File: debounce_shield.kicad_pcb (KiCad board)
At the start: 2 copper layers, 65 x 56 mm, 39 parts, among them J2 RPi_GPIO, P1 CONN_12, P2 CONN_2, U1 40106

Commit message: Add HAT EEPROM & 5V feed diode.
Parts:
- added D7: DIODE, Diodes_SMD:D_0805, F.Cu at (153.0, 81.0)
- added K1: CONN_3, Pin_Headers:Pin_Header_Straight_1x03_Pitch2.54mm, F.Cu at (106.3, 94.5)
- added R19: 1k, Resistors_SMD:R_0805_HandSoldering, F.Cu at (107.8, 82.9)
- added U2: CAT24C32, SMD_Packages:SOIC-8-N, F.Cu at (112.8, 91.6)
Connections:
- J2 pad 2: Net-(J2-Pad2) -> Net-(D7-Pad2)
- J2 pad 27: (no net) -> IDSDA
- J2 pad 28: (no net) -> IDSCL
- J2 pad 4: Net-(J2-Pad2) -> Net-(D7-Pad2)
- P2 pad 2: Net-(J2-Pad2) -> Net-(D7-Pad1)
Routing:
- net Net-(D7-Pad2): track 0.00 -> 62.6 mm
- net Net-(J2-Pad2): track 60.2 -> 0.00 mm
- net IDSCL: track 0.00 -> 40.2 mm, vias 0 -> 1
- net IDSDA: track 0.00 -> 29.1 mm, vias 0 -> 3
- net GND: track 12.5 -> 38.8 mm, vias 7 -> 8
- net +3.3V: track 119.9 -> 105.1 mm
- net Net-(K1-Pad2): track 0.00 -> 8.88 mm
- net Net-(K1-Pad3): track 0.00 -> 6.59 mm
- net Net-(D7-Pad1): track 0.00 -> 4.68 mm
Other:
- net class Power5V added: clearance 0.2, trace_width 0.6, via_dia 0.6, via_drill 0.4

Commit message: Update documentation.
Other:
- board text added: "Wr - WP"
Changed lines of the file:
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@@
     (links 89)
     (no_connects 0)
-    (area 87.089172 61.3852 190.182029 141.5602)
+    (area 97.460599 72.493818 162.560601 128.635201)
     (thickness 1.6)
-    (drawings 28)
+    (drawings 29)
     (tracks 303)
     (zones 0)
@@
   )
   (setup
-    (last_trace_width 0.6)
+    (last_trace_width 0.25)
     (user_trace_width 0.01)
     (user_trace_width 0.02)
@@
       (rotate (xyz 0 0 0))
     )
+  )
+  (gr_text "Wr - WP" (at 108.8898 92.0877 90) (layer F.SilkS)
+    (effects (font (size 1 1) (thickness 0.2)))
   )
   (gr_text "GND +5V" (at 161.798 83.6549 90) (layer F.SilkS)
@@
   (segment (start 153.1788 82.1817) (end 153.0096 82.0125) (width 0.6) (layer F.Cu) (net 31))
   (segment (start 109.9693 73.0885) (end 155.6131 73.0885) (width 0.6) (layer F.Cu) (net 32))
-  (segment (start 155.2788 79.9125) (end 153.0096 79.9125) (width 0.6) (layer F.Cu) (net 32) (status 800000))
+  (segment (start 155.2788 79.9125) (end 153.0096 79.9125) (width 0.6) (layer F.Cu) (net 32))
   (segment (start 155.6004 79.5909) (end 155.2788 79.9125) (width 0.6) (layer F.Cu) (net 32))
   (segment (start 155.6004 73.1012) (end 155.6004 79.5909) (width 0.6) (layer F.Cu) (net 32))

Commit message: Add ID_SC, ID_SD pull-up resistors.
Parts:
- added R20: 3.9k, Resistors_SMD:R_0805_HandSoldering, F.Cu at (111.6, 84.3)
- added R21: 3.9k, Resistors_SMD:R_0805_HandSoldering, F.Cu at (116.1, 84.2)
- moved R19 3.86 mm to (104.3, 84.4), turned to 90 degrees
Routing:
- net +3.3V: track 105.1 -> 114.8 mm
- net IDSDA: track 29.1 -> 32.8 mm
- net IDSCL: track 40.2 -> 43.3 mm
- net Net-(K1-Pad3): track 6.59 -> 4.50 mm

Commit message: Clarify label for EEPROM WP pin header.
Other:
- board text added: "WE - WP"
- board text removed: "Wr - WP"
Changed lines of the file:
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@@
     (links 93)
     (no_connects 0)
-    (area 87.089172 61.3852 190.182029 141.5602)
+    (area 97.460599 72.493818 162.560601 128.635201)
     (thickness 1.6)
     (drawings 29)
@@
     )
   )
-  (gr_text "Wr - WP" (at 108.8898 92.0877 90) (layer F.SilkS)
+  (gr_text "WE - WP" (at 108.8898 92.0877 90) (layer F.SilkS)
     (effects (font (size 1 1) (thickness 0.2)))
   )
@@
   (segment (start 153.1928 117.8052) (end 157.5181 117.8052) (width 0.25) (layer F.Cu) (net 19))
   (segment (start 157.5181 117.8052) (end 157.5308 117.7925) (width 0.25) (layer F.Cu) (net 19))
-  (segment (start 104.2797 83.0796) (end 104.2797 80.9244) (width 0.25) (layer F.Cu) (net 20) (status 400000))
+  (segment (start 104.2797 83.0796) (end 104.2797 80.9244) (width 0.25) (layer F.Cu) (net 20))
   (segment (start 104.2797 80.9244) (end 105.9307 79.2734) (width 0.25) (layer F.Cu) (net 20))
-  (segment (start 111.633 82.9653) (end 110.6602 82.9653) (width 0.25) (layer F.Cu) (net 20) (status 400000))
+  (segment (start 111.633 82.9653) (end 110.6602 82.9653) (width 0.25) (layer F.Cu) (net 20))
   (segment (start 110.6602 82.9653) (end 109.9058 82.2109) (width 0.25) (layer F.Cu) (net 20))
   (segment (start 116.0526 82.8891) (end 116.0526 79.9338) (width 0.25) (layer F.Cu) (net 20))
@@
   (segment (start 116.3955 87.5665) (end 115.5446 88.4174) (width 0.25) (layer F.Cu) (net 27))
   (segment (start 115.5446 88.4174) (end 114.7191 88.4174) (width 0.25) (layer F.Cu) (net 27))
-  (segment (start 111.633 85.6653) (end 112.1448 85.6653) (width 0.25) (layer F.Cu) (net 28) (status C00000))
-  (segment (start 112.1448 85.6653) (end 113.4237 86.9442) (width 0.25) (layer F.Cu) (net 28) (status 400000))
+  (segment (start 111.633 85.6653) (end 112.1448 85.6653) (width 0.25) (layer F.Cu) (net 28))
+  (segment (start 112.1448 85.6653) (end 113.4237 86.9442) (width 0.25) (layer F.Cu) (net 28))
   (segment (start 113.4237 86.9442) (end 113.4237 87.7443) (width 0.25) (layer F.Cu) (net 28))
   (segment (start 113.4237 87.7443) (end 113.4491 87.7443) (width 0.25) (layer F.Cu) (net 28))
@@
   (segment (start 112.1791 91.0082) (end 112.1791 88.4174) (width 0.25) (layer F.Cu) (net 29))
   (segment (start 111.2012 91.9861) (end 112.1791 91.0082) (width 0.25) (layer F.Cu) (net 29))
-  (segment (start 104.2797 85.7796) (end 104.2797 87.4268) (width 0.25) (layer F.Cu) (net 30) (status 400000))
-  (segment (start 104.2797 87.4268) (end 106.299 89.4461) (width 0.25) (layer F.Cu) (net 30) (status 800000))
+  (segment (start 104.2797 85.7796) (end 104.2797 87.4268) (width 0.25) (layer F.Cu) (net 30))
+  (segment (start 104.2797 87.4268) (end 106.299 89.4461) (width 0.25) (layer F.Cu) (net 30))
   (segment (start 157.6197 82.1817) (end 153.1788 82.1817) (width 0.6) (layer F.Cu) (net 31))
   (segment (start 153.1788 82.1817) (end 153.0096 82.0125) (width 0.6) (layer F.Cu) (net 31))

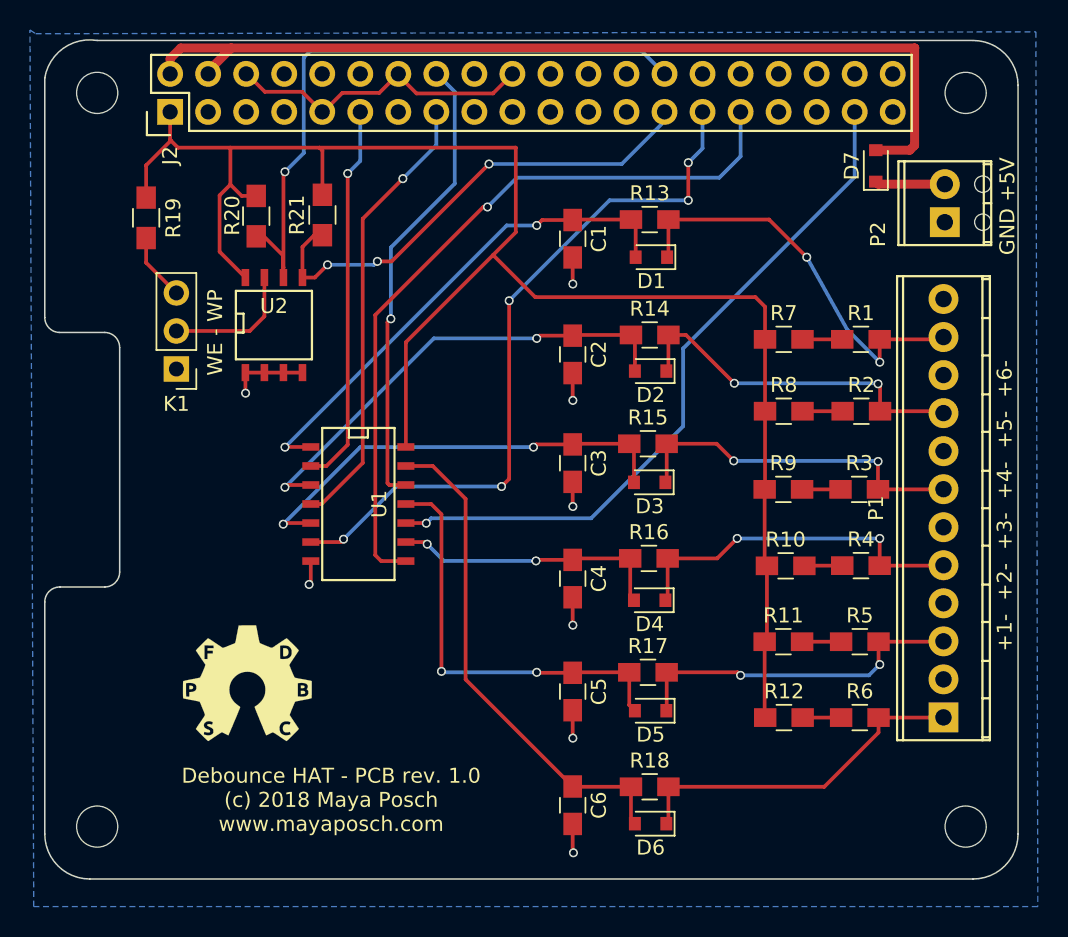
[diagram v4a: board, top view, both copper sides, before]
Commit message: Add optocoupler & other improvements.
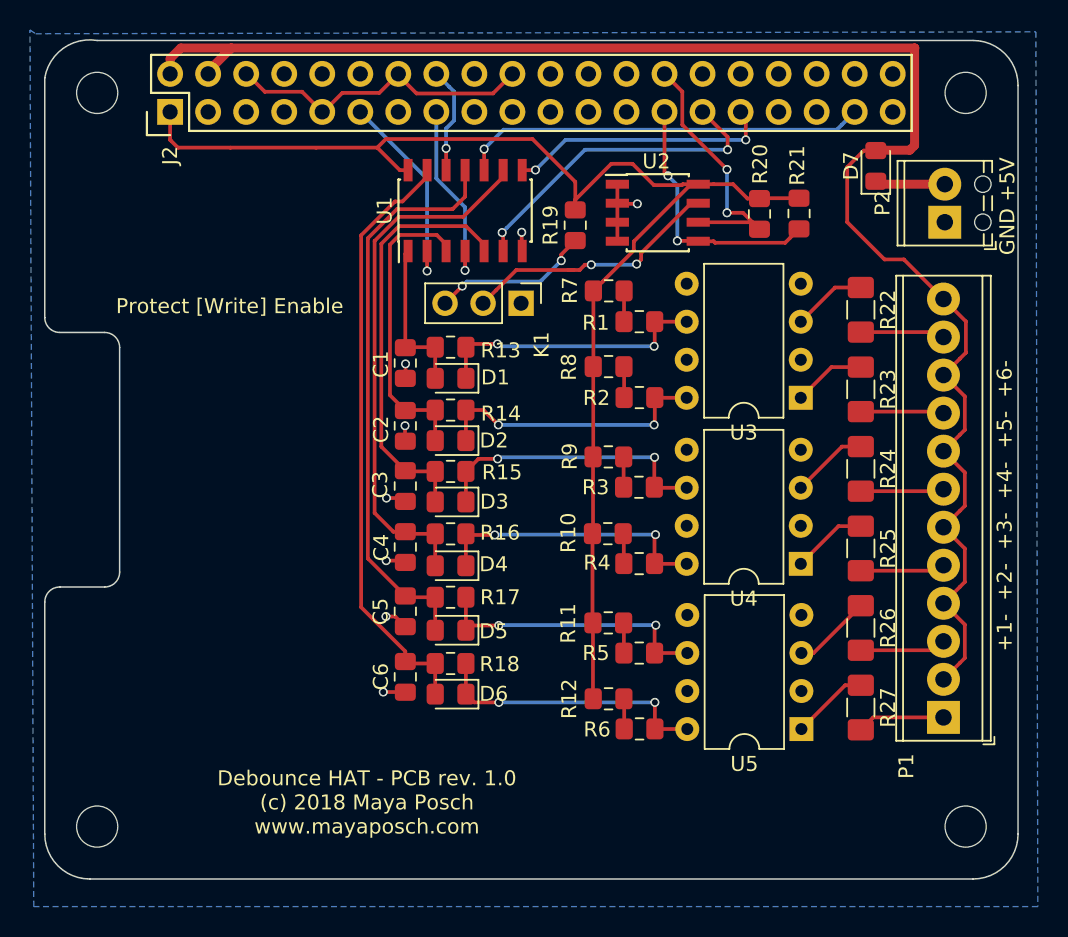
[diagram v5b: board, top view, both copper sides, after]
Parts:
- removed G***: LOGO, oshw:oshw
- added R22: 191, Resistor_SMD:R_1206_3216Metric_Pad1.42x1.75mm_HandSolder, F.Cu at (152.0, 90.6)
- added R23: 191, Resistor_SMD:R_1206_3216Metric_Pad1.42x1.75mm_HandSolder, F.Cu at (152.0, 95.9)
- added R24: 191, Resistor_SMD:R_1206_3216Metric_Pad1.42x1.75mm_HandSolder, F.Cu at (152.0, 101.2)
- added R25: 191, Resistor_SMD:R_1206_3216Metric_Pad1.42x1.75mm_HandSolder, F.Cu at (152.0, 106.5)
- added R26: 191, Resistor_SMD:R_1206_3216Metric_Pad1.42x1.75mm_HandSolder, F.Cu at (152.0, 111.8)
- added R27: 191, Resistor_SMD:R_1206_3216Metric_Pad1.42x1.75mm_HandSolder, F.Cu at (152.0, 117.1)
- added U3: LTV-824, Package_DIP:DIP-8_W7.62mm, F.Cu at (148.0, 96.4)
- added U4: LTV-824, Package_DIP:DIP-8_W7.62mm, F.Cu at (148.0, 107.5)
- added U5: LTV-824, Package_DIP:DIP-8_W7.62mm, F.Cu at (148.0, 118.6)
- C1, C2, C3, C4, C5, C6: footprint Capacitors_SMD:C_0805_HandSoldering -> Capacitor_SMD:C_0805_2012Metric_Pad1.15x1.40mm_HandSolder
- D1, D2, D3, D4, D5, D6, D7: footprint Diodes_SMD:D_0805 -> Diode_SMD:D_0805_2012Metric_Pad1.15x1.40mm_HandSolder
- K1: footprint Pin_Headers:Pin_Header_Straight_1x03_Pitch2.54mm -> Connector_PinHeader_2.54mm:PinHeader_1x03_P2.54mm_Vertical
- P1: footprint TerminalBlocks_Phoenix:TerminalBlock_Phoenix_MPT-2.54mm_12pol -> TerminalBlock_Phoenix:TerminalBlock_Phoenix_MPT-0,5-12-2.54_1x12_P2.54mm_Horizontal
- P2: footprint TerminalBlocks_Phoenix:TerminalBlock_Phoenix_MPT-2.54mm_2pol -> TerminalBlock_Phoenix:TerminalBlock_Phoenix_MPT-0,5-2-2.54_1x02_P2.54mm_Horizontal
- R1, R10, R11, R12, R13, R14, R15, R16, R17, R18, R2, R3, R4, R5, R6, R7, R8, R9: footprint Capacitors_SMD:C_0805_HandSoldering -> Resistor_SMD:R_0805_2012Metric_Pad1.15x1.40mm_HandSolder
- R19, R20, R21: footprint Resistors_SMD:R_0805_HandSoldering -> Resistor_SMD:R_0805_2012Metric_Pad1.15x1.40mm_HandSolder
- U1: footprint SMD_Packages:SOIC-14_N -> Package_SO:SOIC-14_3.9x8.7mm_P1.27mm
- U2: footprint SMD_Packages:SOIC-8-N -> Package_SO:SOIC-8_3.9x4.9mm_P1.27mm
- moved R20 33.6 mm to (145.2, 84.2)
- moved R21 31.8 mm to (147.9, 84.1)
- moved R19 28.7 mm to (132.9, 84.9)
- moved U2 26.7 mm to (138.5, 84.1)
- moved K1 23.4 mm to (129.3, 90.1), turned to 270 degrees
- moved U1 20.8 mm to (125.6, 83.9), turned to 90 degrees
- moved D6 15.9 mm to (124.6, 116.2)
- moved R13 15.8 mm to (124.6, 93.1)
- moved D1 15.7 mm to (124.6, 95.1)
- moved R18 15.6 mm to (124.6, 114.2)
- moved R2 14.8 mm to (137.2, 96.4)
- moved R1 14.8 mm to (137.2, 91.4)
- moved R4 14.8 mm to (137.2, 107.5)
- moved R5 14.8 mm to (137.2, 113.5)
- moved R6 14.7 mm to (137.2, 118.6)
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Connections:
- D7 pad 2: Net-(D7-Pad2) -> +5V
- J2 pad 10: (no net) -> Net-(J2-Pad10)
- J2 pad 12: (no net) -> Net-(J2-Pad12)
- J2 pad 13: (no net) -> Net-(J2-Pad13)
- J2 pad 17: (no net) -> Net-(J2-Pad17)
- J2 pad 18: (no net) -> Net-(J2-Pad18)
- J2 pad 19: (no net) -> Net-(J2-Pad19)
- J2 pad 2: Net-(D7-Pad2) -> +5V
- J2 pad 21: (no net) -> Net-(J2-Pad21)
- J2 pad 22: (no net) -> Net-(J2-Pad22)
- J2 pad 23: (no net) -> Net-(J2-Pad23)
- J2 pad 24: (no net) -> Net-(J2-Pad24)
- J2 pad 25: (no net) -> Net-(J2-Pad25)
- J2 pad 26: (no net) -> Net-(J2-Pad26)
- J2 pad 3: (no net) -> Net-(J2-Pad3)
- J2 pad 32: (no net) -> Net-(J2-Pad32)
- J2 pad 33: (no net) -> Net-(J2-Pad33)
- J2 pad 35: (no net) -> Net-(J2-Pad35)
- J2 pad 36: (no net) -> Net-(J2-Pad36)
- J2 pad 38: (no net) -> Net-(J2-Pad38)
- J2 pad 4: Net-(D7-Pad2) -> +5V
- J2 pad 40: (no net) -> Net-(J2-Pad40)
- J2 pad 5: (no net) -> Net-(J2-Pad5)
- J2 pad 7: (no net) -> Net-(J2-Pad7)
- J2 pad 8: (no net) -> Net-(J2-Pad8)
- P1 pad 1: Net-(D6-Pad1) -> Net-(P1-Pad1)
- P1 pad 10: GND -> +5V
- P1 pad 11: Net-(D1-Pad1) -> Net-(P1-Pad11)
- P1 pad 12: GND -> +5V
- P1 pad 2: GND -> +5V
- P1 pad 3: Net-(D5-Pad1) -> Net-(P1-Pad3)
- P1 pad 4: GND -> +5V
- P1 pad 5: Net-(D4-Pad1) -> Net-(P1-Pad5)
- P1 pad 6: GND -> +5V
- P1 pad 7: Net-(D3-Pad1) -> Net-(P1-Pad7)
- P1 pad 8: GND -> +5V
- P1 pad 9: Net-(D2-Pad1) -> Net-(P1-Pad9)
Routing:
- net +5V: track 0.00 -> 108.6 mm
- net Net-(D7-Pad2): track 62.6 -> 0.00 mm
- net Net-(J2-Pad31): track 50.0 -> 17.8 mm, vias 1 -> 2
- net Net-(J2-Pad29): track 47.9 -> 21.8 mm, vias 5 -> 2
- net IDSCL: track 43.3 -> 17.9 mm, vias 1 -> 2
- net +3.3V: track 114.8 -> 90.3 mm
- net Net-(J2-Pad16): track 31.0 -> 7.15 mm
- net Net-(C1-Pad1): track 33.8 -> 10.6 mm, vias 2 -> 0
- net Net-(J2-Pad37): track 46.9 -> 27.2 mm
- net Net-(J2-Pad15): track 30.1 -> 12.7 mm
- net Net-(C4-Pad1): track 18.5 -> 35.7 mm, vias 2 -> 0
- net IDSDA: track 32.8 -> 17.5 mm, vias 3 -> 2
- net Net-(J2-Pad11): track 25.6 -> 13.8 mm
- net Net-(C2-Pad1): track 31.6 -> 20.3 mm, vias 2 -> 0
- net Net-(C5-Pad1): track 28.5 -> 38.6 mm, vias 2 -> 0
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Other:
- board text added: "Protect [Write] Enable"
- board text removed: "WE - WP"

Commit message: Added fiducials. Tweaked traces & silkscreen.
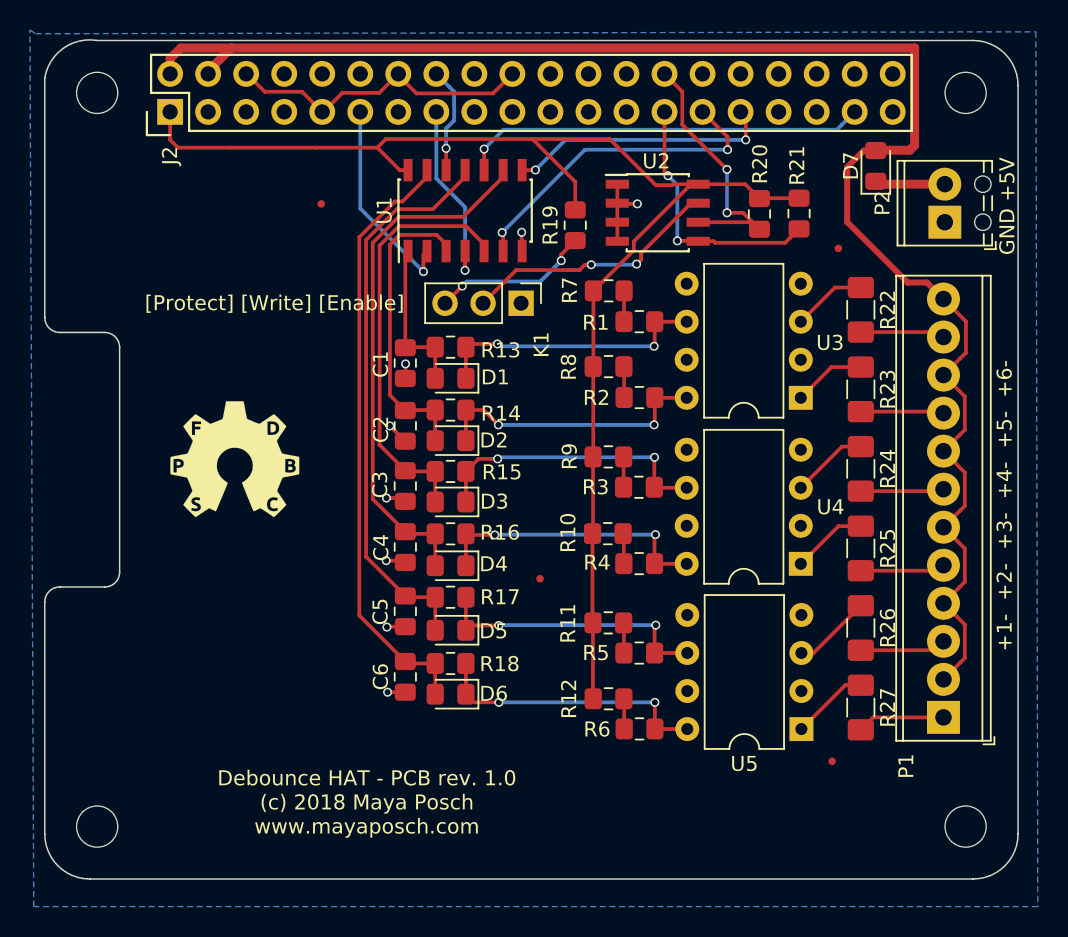
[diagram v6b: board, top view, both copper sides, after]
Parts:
- added G***: LOGO, oshw:oshw, F.Cu at (110.3, 100.7)
- added REF**: Fiducial_0.5mm_Dia_1mm_Outer, Fiducial:Fiducial_0.5mm_Dia_1mm_Outer, F.Cu at (150.1, 120.7)
- added REF**: Fiducial_0.5mm_Dia_1mm_Outer, Fiducial:Fiducial_0.5mm_Dia_1mm_Outer, F.Cu at (130.6, 108.5)
- added REF**: Fiducial_0.5mm_Dia_1mm_Outer, Fiducial:Fiducial_0.5mm_Dia_1mm_Outer, F.Cu at (150.5, 86.5)
- added REF**: Fiducial_0.5mm_Dia_1mm_Outer, Fiducial:Fiducial_0.5mm_Dia_1mm_Outer, F.Cu at (116.0, 83.5)
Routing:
- net +3.3V: track 90.3 -> 92.2 mm
- net Net-(C5-Pad1): track 38.6 -> 37.9 mm
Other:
- board text added: "[Protect] [Write] [Enable]"
- board text removed: "Protect [Write] Enable"
